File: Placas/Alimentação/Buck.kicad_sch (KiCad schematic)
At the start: 5 parts, among them J5 Conn_01x01_Pin, J6 Conn_01x01_Pin, J7 Conn_01x01_Pin, J8 Conn_01x01_Pin, U1 YAAJ_DCDC_StepDown_LM2596

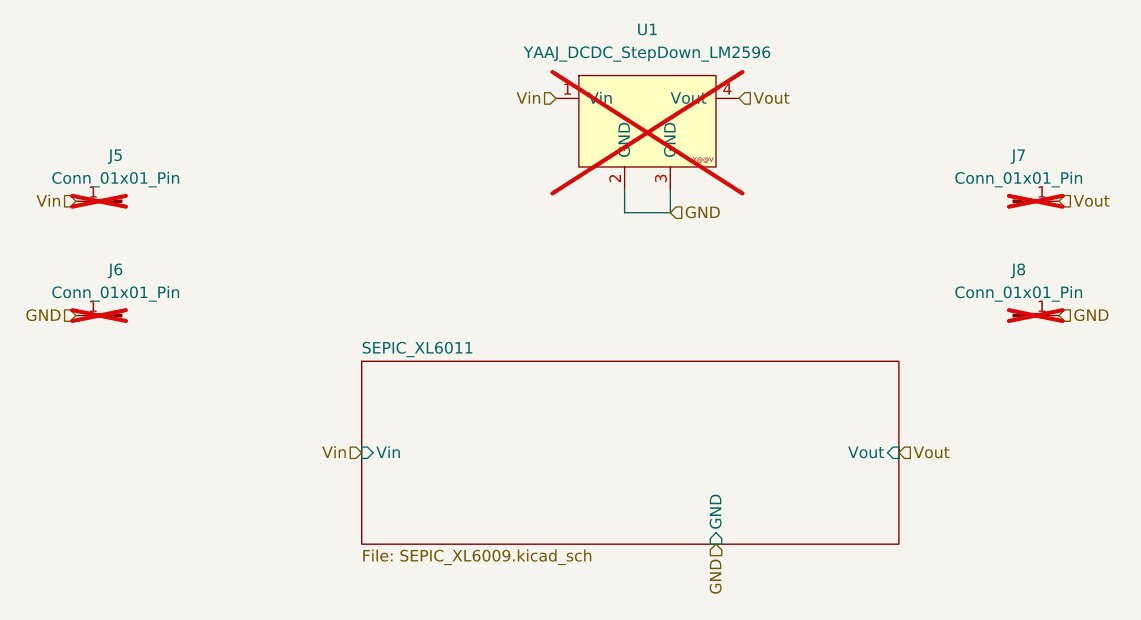
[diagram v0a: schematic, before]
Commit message: Modificações nas duas placas, adição de furos para montagem, melhora na posição dos micros e conectores para comunicação SPI
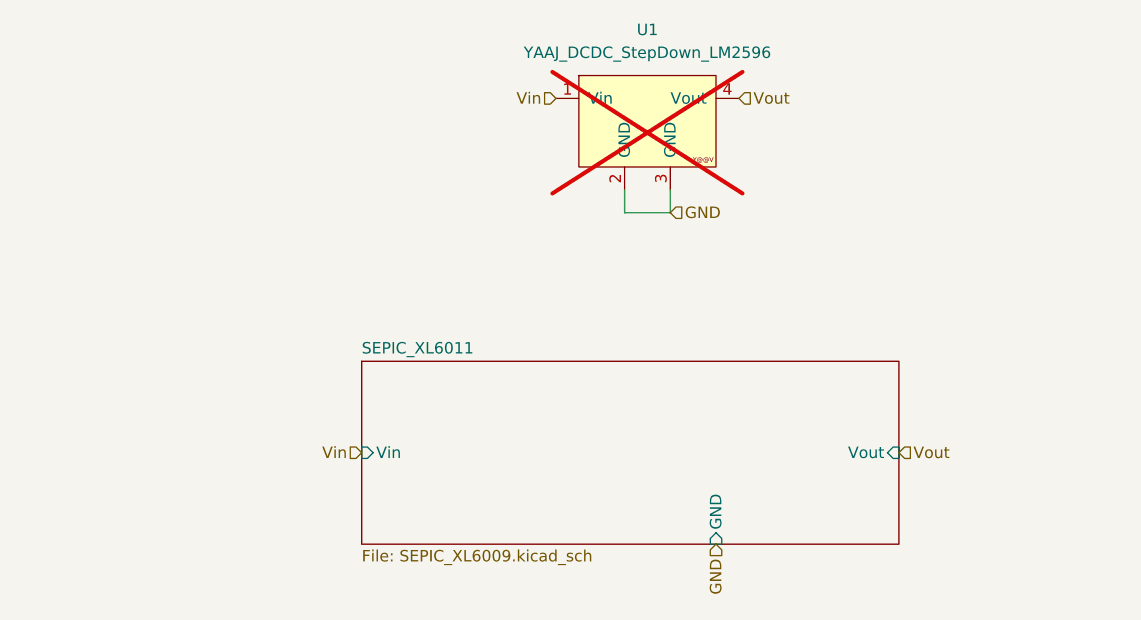
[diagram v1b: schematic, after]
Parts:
- removed J5, J6, J7, J8: Conn_01x01_Pin, Connector_PinHeader_2.54mm:PinHeader_1x01_P2.54mm_Vertical, symbol Connector:Conn_01x01_Pin

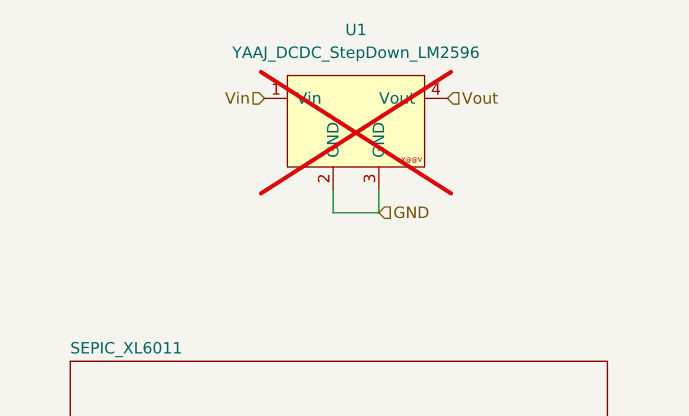
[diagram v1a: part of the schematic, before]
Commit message: Criação dos arquivos em C para o firmware dos dois micros e script em python para salvar aquisição dos dados e envio de comandos
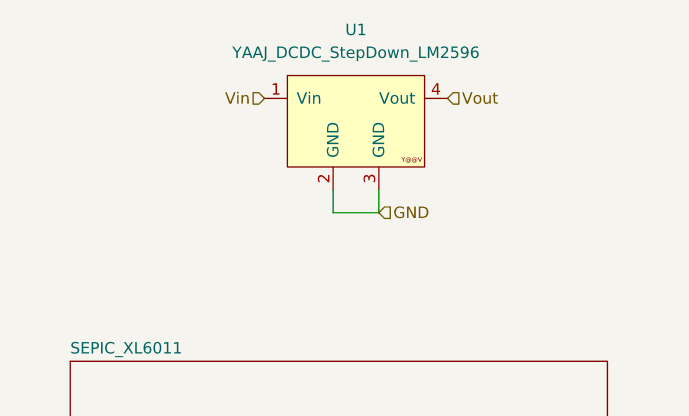
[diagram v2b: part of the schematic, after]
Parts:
- U1: now fitted
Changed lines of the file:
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@@
 		(in_bom yes)
 		(on_board yes)
-		(dnp yes)
+		(dnp no)
 		(fields_autoplaced yes)
 		(property "Reference" "U1"
